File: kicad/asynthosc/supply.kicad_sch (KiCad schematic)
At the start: 51 parts, among them J1 USB_B_Micro, J17 Conn_01x02, J2 Conn_02x05_Odd_Even, U1 LM1117S-3.3, U2 LMR62421XMF, U3 USBLC6-2SC6, U4 LM1117S-5.0, U5 Si1869DH

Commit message: pcb: add design rules to match jlc pcba assembly rules. sch: fix a 0805 package mishap
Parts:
- C1, C4: footprint Capacitor_SMD:C_01005_0402Metric -> Capacitor_SMD:C_0805_2012Metric
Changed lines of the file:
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@@
 			)
 		)
-		(property "Footprint" "Capacitor_SMD:C_01005_0402Metric"
+		(property "Footprint" "Capacitor_SMD:C_0805_2012Metric"
 			(at 40.3352 96.52 0)
 			(effects
@@
 			)
 		)
-		(property "Footprint" "Capacitor_SMD:C_01005_0402Metric"
+		(property "Footprint" "Capacitor_SMD:C_0805_2012Metric"
 			(at 69.5452 96.52 0)
 			(effects

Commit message: bom: update mfr, serials and lcsc fields
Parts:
- C12, C3, C5: LCSC (none) -> C72485
- D1, D3: LCSC (none) -> C111566
- D2: LCSC (none) -> C2921026; Manufacturer Guangdong -> Agertech
- D4, D5, D6: LCSC (none) -> C3014007
- FB1: LCSC (none) -> C160974
- J1: LCSC (none) -> C5160321
- J2: LCSC (none) -> C3294463; Manufacturer (none) -> HCTL; RefNum _na_ -> PZ254-2-05-S
- L1: LCSC (none) -> C7462918
- TH1: LCSC (none) -> C2935581; Manufacturer (none) -> Ruilon; RefNum _generic_ -> NTC16D-9
- U1: LCSC (none) -> C126027
- U2: LCSC (none) -> C2070685
- U3: LCSC (none) -> C7519
- U4: LCSC (none) -> C126028
- U5: LCSC (none) -> C128638; Manufacturer (none) -> Vishay
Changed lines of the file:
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@@
 			)
 		)
-		(property "LCSC" ""
+		(property "LCSC" "C2070685 "
 			(at 59.69 190.5 0)
 			(effects
@@
 			)
 		)
-		(property "LCSC" ""
+		(property "LCSC" "C72485"
 			(at 41.91 180.34 0)
 			(effects
@@
 			)
 		)
-		(property "LCSC" ""
+		(property "LCSC" "C72485"
 			(at 80.01 259.08 0)
 			(effects
@@
 			)
 		)
-		(property "LCSC" ""
+		(property "LCSC" "C126028"
 			(at 105.41 255.27 0)
 			(effects
@@
 			)
 		)
-		(property "LCSC" ""
+		(property "LCSC" "C3014007"
 			(at 198.12 43.18 0)
 			(effects
@@
 			)
 		)
-		(property "LCSC" ""
+		(property "LCSC" "C126027"
 			(at 53.34 88.9 0)
 			(effects
@@
 			)
 		)
-		(property "LCSC" ""
+		(property "LCSC" "C128638"
 			(at 200.66 257.81 0)
 			(effects
@@
 			)
 		)
-		(property "Manufacturer" ""
+		(property "Manufacturer" "Vishay"
 			(at 200.66 257.81 0)
 			(effects
@@
 			)
 		)
-		(property "LCSC" ""
+		(property "LCSC" "C3294463"
 			(at 44.45 257.81 0)
 			(effects
@@
 			)
 		)
-		(property "Manufacturer" ""
+		(property "Manufacturer" "HCTL"
 			(at 44.45 257.81 0)
 			(effects
@@
 			)
 		)
-		(property "RefNum" "_na_"
+		(property "RefNum" "PZ254-2-05-S"
 			(at 44.45 257.81 0)
 			(effects
@@
 			)
 		)
-		(property "LCSC" ""
+		(property "LCSC" "C111566"
 			(at 67.31 57.15 0)
 			(effects
@@
 			)
 		)
-		(property "LCSC" ""
+		(property "LCSC" "C111566"
 			(at 77.47 57.15 0)
 			(effects
@@
 			)
 		)
-		(property "LCSC" ""
+		(property "LCSC" "C3014007"
 			(at 81.28 172.72 0)
 			(effects
@@
 			)
 		)
-		(property "LCSC" ""
+		(property "LCSC" "C72485"
 			(at 189.23 46.99 0)
 			(effects
@@
 			)
 		)
-		(property "RefNum" "_generic_"
+		(property "RefNum" "NTC16D-9"
 			(at 144.78 43.18 0)
 			(effects
@@
 			)
 		)
-		(property "LCSC" ""
+		(property "LCSC" "C2935581"
 			(at 144.78 43.18 0)
 			(effects
@@
 			)
 		)
-		(property "Manufacturer" ""
+		(property "Manufacturer" "Ruilon"
 			(at 144.78 43.18 0)
 			(effects
@@
 			)
 		)
-		(property "LCSC" ""
+		(property "LCSC" "C7462918"
 			(at 58.42 172.72 0)
 			(effects
@@
 			)
 		)
-		(property "LCSC" ""
+		(property "LCSC" "C7519"
 			(at 62.23 143.51 0)
 			(effects
@@
 			)
 		)
-		(property "LCSC" ""
+		(property "LCSC" "C3014007"
 			(at 133.35 248.92 0)
 			(effects
@@
 			)
 		)
-		(property "LCSC" ""
+		(property "LCSC" "C2921026"
 			(at 67.31 248.92 0)
 			(effects
@@
 			)
 		)
-		(property "Manufacturer" "Guangdong"
+		(property "Manufacturer" "Agertech"
 			(at 67.31 248.92 0)
 			(effects
@@
 			)
 		)
-		(property "LCSC" ""
+		(property "LCSC" "C160974"
 			(at 165.1 43.18 0)
 			(effects
@@
 			)
 		)
-		(property "LCSC" ""
+		(property "LCSC" "C5160321"
 			(at 40.64 43.18 0)
 			(effects

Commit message: bom: sch: pcb: update for sourcing in jlc pcba services
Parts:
- U5: LCSC C128638 -> C5246384; Manufacturer Vishay -> Tech Public; RefNum Si1869DH -> TPSI1869DH-T1-E3
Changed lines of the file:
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@@
 			)
 		)
-		(property "LCSC" "C128638"
+		(property "LCSC" "C5246384"
 			(at 200.66 257.81 0)
 			(effects
@@
 			)
 		)
-		(property "Manufacturer" "Vishay"
+		(property "Manufacturer" "Tech Public"
 			(at 200.66 257.81 0)
 			(effects
@@
 			)
 		)
-		(property "RefNum" "Si1869DH"
+		(property "RefNum" "TPSI1869DH-T1-E3"
 			(at 200.66 257.81 0)
 			(effects

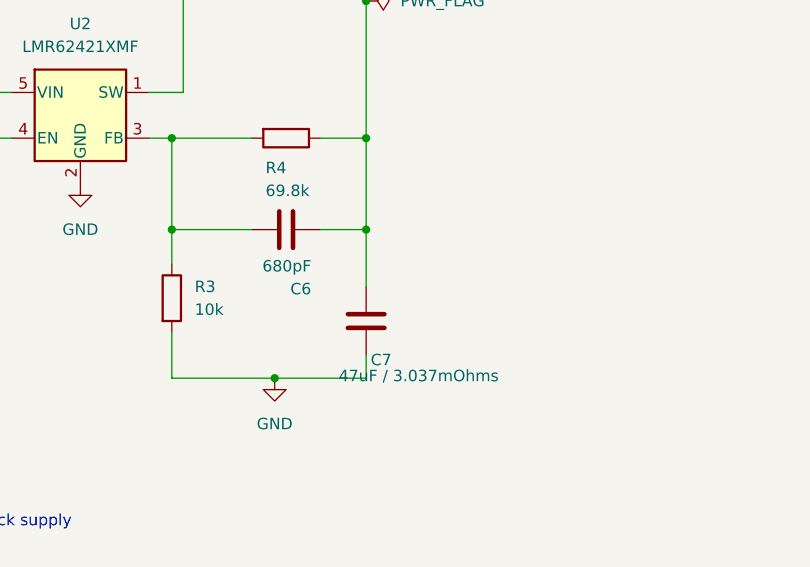
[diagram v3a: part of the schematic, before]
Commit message: bom: update for better bom
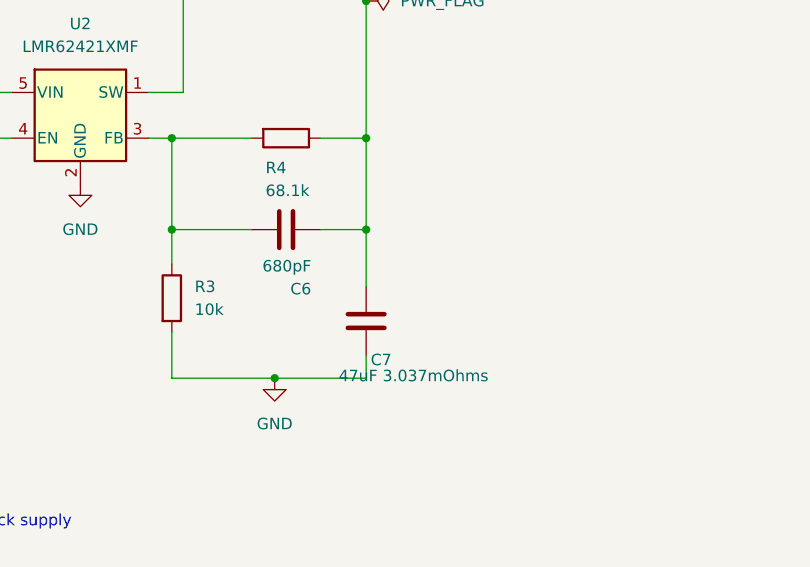
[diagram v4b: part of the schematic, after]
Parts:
- C7: value 47uF / 3.037mOhms -> 47uF 3.037mOhms
- H1, H2, H3, J17: RefNum (none) -> _na_
- R4: value 69.8k -> 68.1k
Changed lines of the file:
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@@
 			)
 		)
-		(property "Value" "47uF / 3.037mOhms"
+		(property "Value" "47uF 3.037mOhms"
 			(at 88.392 219.456 0)
 			(effects
@@
 			)
 		)
+		(property "RefNum" "_na_"
+			(at 138.43 101.6 0)
+			(effects
+				(font
+					(size 1.27 1.27)
+				)
+				(hide yes)
+			)
+		)
 		(pin "1"
 		)
@@
 			)
 		)
+		(property "RefNum" "_na_"
+			(at 106.68 73.66 0)
+			(effects
+				(font
+					(size 1.27 1.27)
+				)
+				(hide yes)
+			)
+		)
 		(pin "2"
 		)
@@
 			)
 		)
+		(property "RefNum" "_na_"
+			(at 133.35 101.6 0)
+			(effects
+				(font
+					(size 1.27 1.27)
+				)
+				(hide yes)
+			)
+		)
 		(pin "1"
 		)
@@
 			)
 		)
-		(property "Value" "69.8k"
+		(property "Value" "68.1k"
 			(at 80.264 198.882 90)
 			(effects
@@
 			(at 143.51 101.6 0)
 			(effects
+				(font
+					(size 1.27 1.27)
+				)
+				(hide yes)
+			)
+		)
+		(property "RefNum" "_na_"
+			(at 143.51 101.6 0)
+			(effects

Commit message: bom: add jlcpcb field with simplified footprint
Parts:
- C1, C2, C4, C7, C8, C9, F1: JLC (none) -> 0805
- C10, C11, C6, R1, R2, R3, R4, R5, R6: JLC (none) -> 0402
- D1, D3: JLC (none) -> SOD-923
- D2: JLC (none) -> SOD-323
- D4, D5, D6: JLC (none) -> SMA
- U1, U4: JLC (none) -> SOT-223
- U2: JLC (none) -> SOT-23-5
- U3: JLC (none) -> SOT-23-6
- U5: JLC (none) -> SOT-363

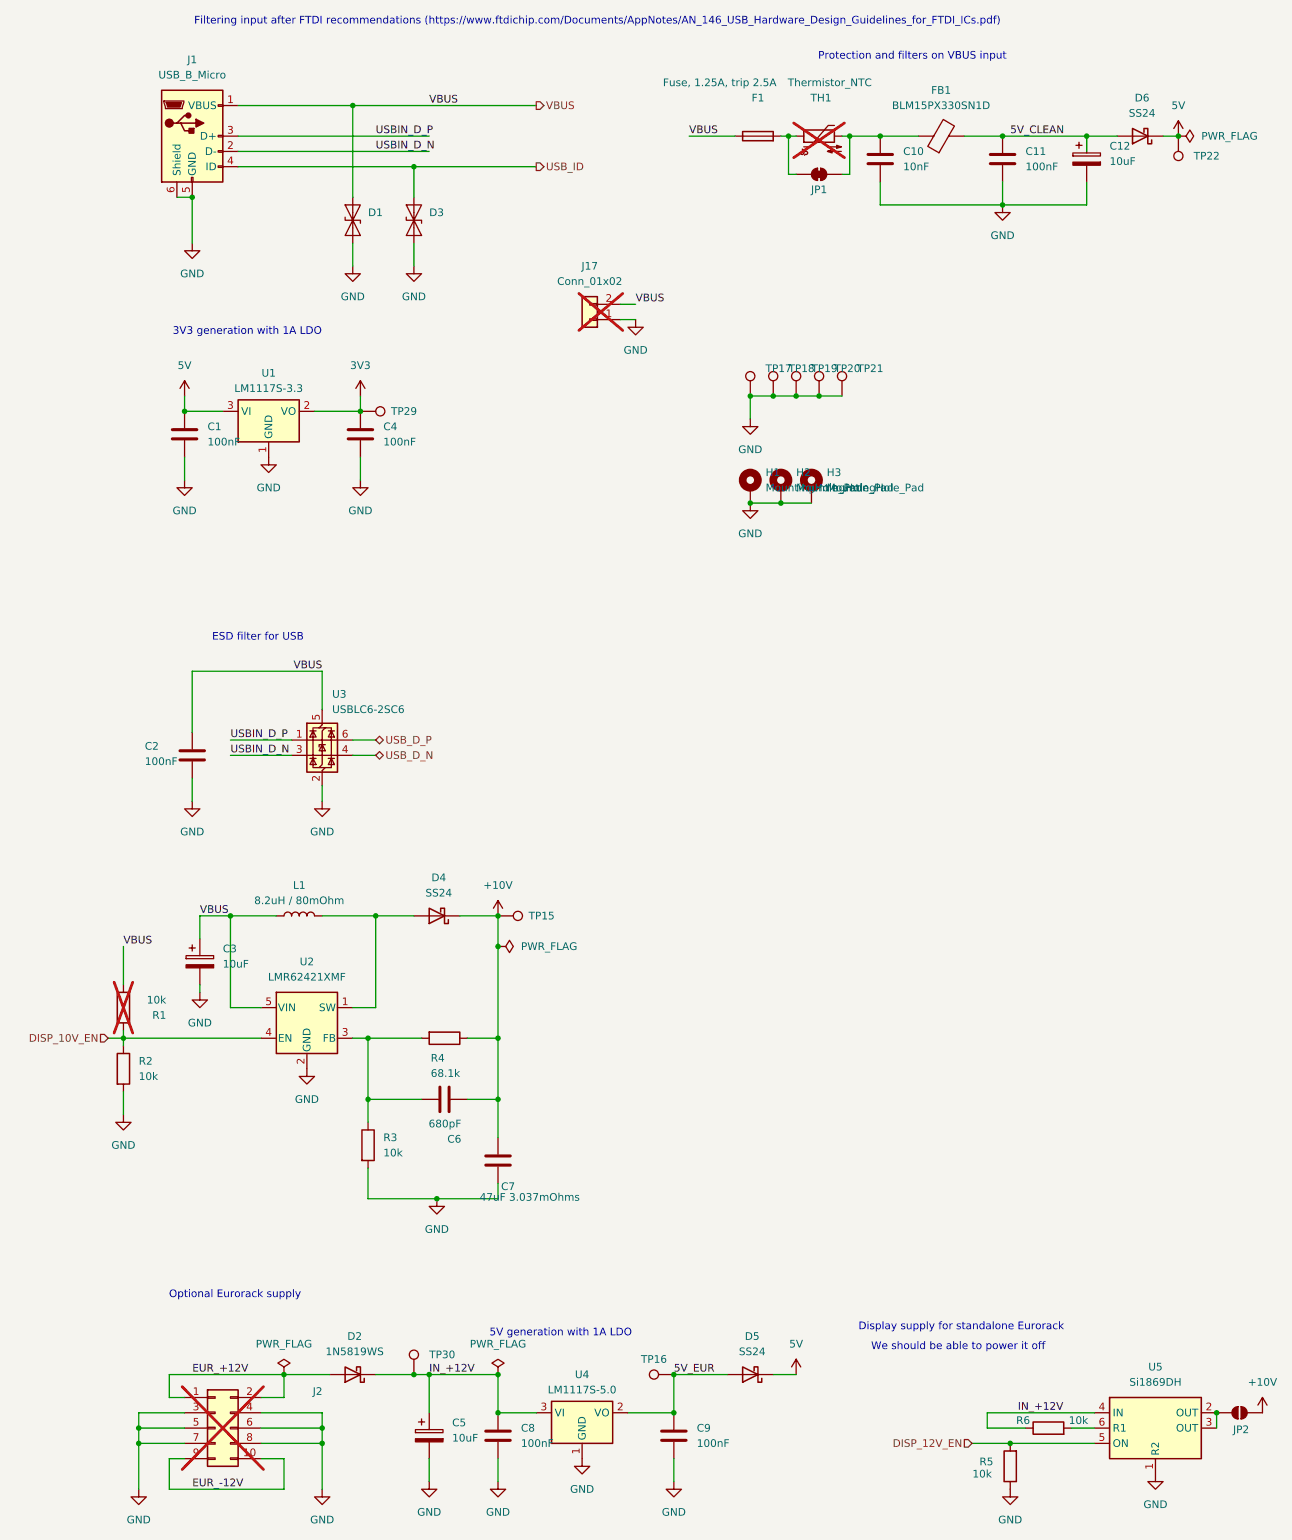
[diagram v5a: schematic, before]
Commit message: bom: dnp for all manually equiped components
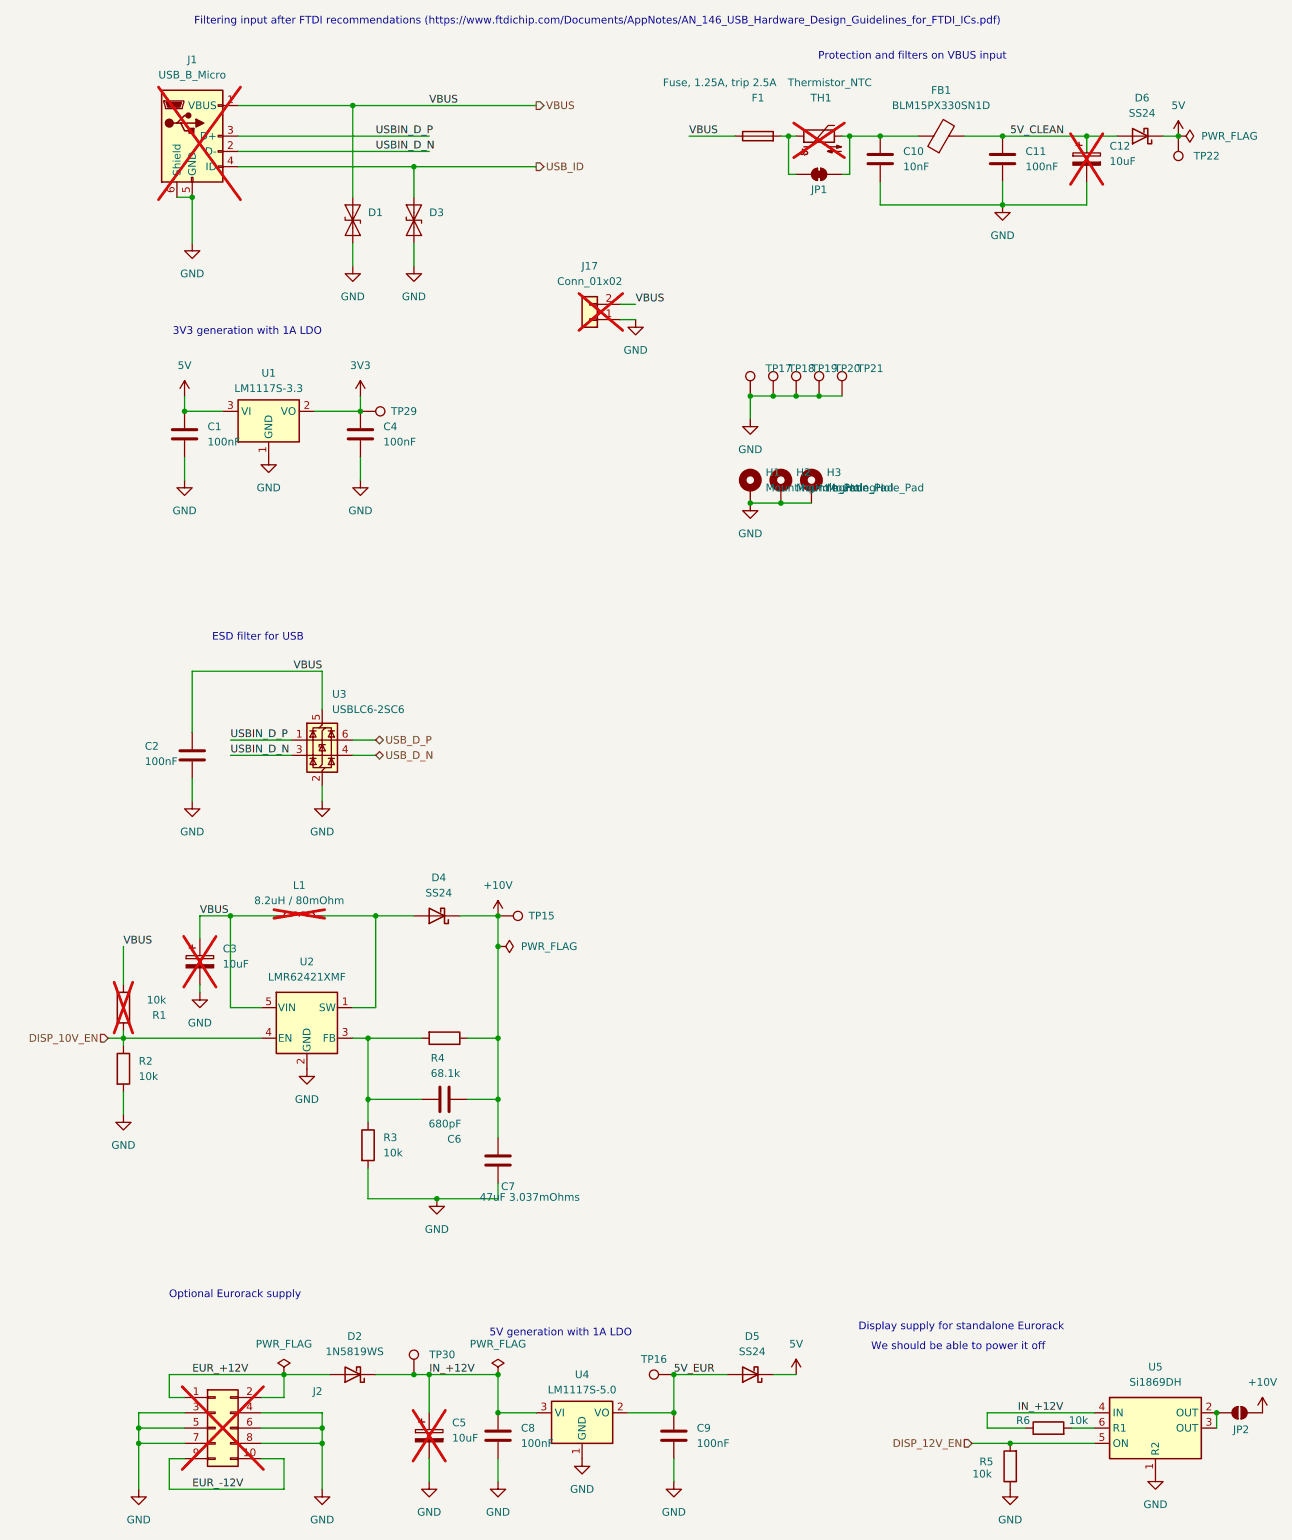
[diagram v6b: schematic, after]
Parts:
- C12, C3, C5, J1, L1: now not fitted
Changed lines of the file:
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@@
 		(in_bom yes)
 		(on_board yes)
-		(dnp no)
+		(dnp yes)
 		(fields_autoplaced yes)
 		(property "Reference" "C3"
@@
 		(in_bom yes)
 		(on_board yes)
-		(dnp no)
+		(dnp yes)
 		(fields_autoplaced yes)
 		(property "Reference" "C5"
@@
 		(in_bom yes)
 		(on_board yes)
-		(dnp no)
+		(dnp yes)
 		(fields_autoplaced yes)
 		(property "Reference" "C12"
@@
 		(in_bom yes)
 		(on_board yes)
-		(dnp no)
+		(dnp yes)
 		(fields_autoplaced yes)
 		(property "Reference" "L1"
@@
 		(in_bom yes)
 		(on_board yes)
-		(dnp no)
+		(dnp yes)
 		(fields_autoplaced yes)
 		(property "Reference" "J1"

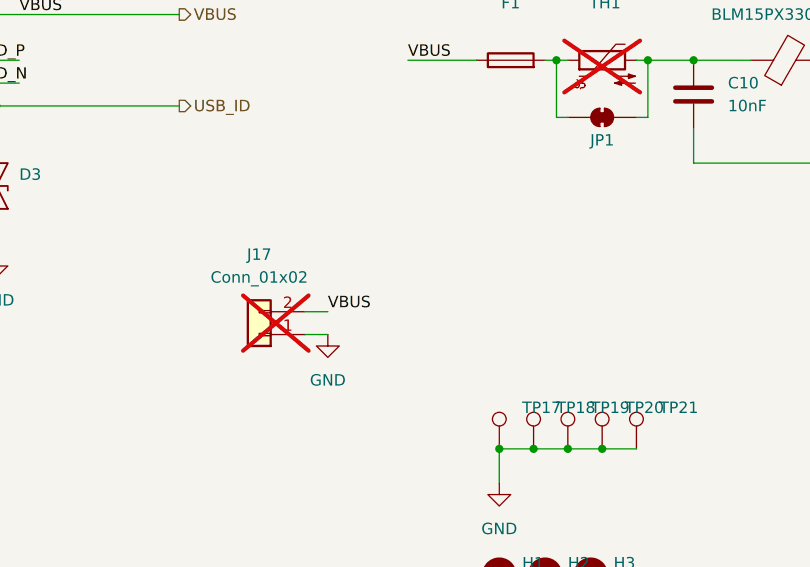
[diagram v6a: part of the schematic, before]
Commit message: sch: pcb: add a diode for external 5V input to protect USB VBUS
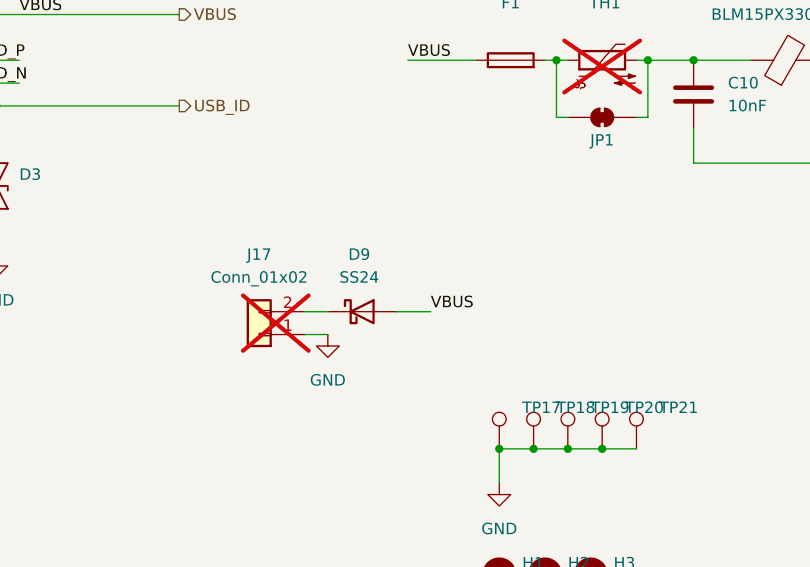
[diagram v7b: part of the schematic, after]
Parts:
- added D9: SS24, Diode_SMD:D_SMA, symbol Diode:SS24
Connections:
- net VBUS: now also D9.2 (A); no longer J17.2 (Pin_2)
- new net: D9.1 (K), J17.2 (Pin_2)
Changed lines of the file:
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@@
 	(wire
 		(pts
+			(xy 125.73 71.12) (xy 121.92 71.12)
+		)
+		(stroke
+			(width 0)
+			(type default)
+		)
+	)
+	(wire
+		(pts
 			(xy 91.44 203.2) (xy 91.44 209.55)
 		)
@@
 	)
 	(label "VBUS"
+		(at 125.73 71.12 0)
+		(fields_autoplaced yes)
+		(effects
+			(font
+				(size 1.27 1.27)
+			)
+			(justify left bottom)
+		)
+	)
+	(label "VBUS"
 		(at 29.21 177.8 0)
 		(fields_autoplaced yes)
@@
 	)
 	(label "VBUS"
-		(at 114.3 71.12 0)
-		(fields_autoplaced yes)
-		(effects
-			(font
-				(size 1.27 1.27)
-			)
-			(justify left bottom)
-		)
-	)
-	(label "VBUS"
 		(at 80.01 38.1 0)
 		(fields_autoplaced yes)
@@
 					(unit 1)
 				)
+			)
+		)
+	)
+	(symbol
+		(lib_id "Diode:SS24")
+		(at 118.11 71.12 0)
+		(unit 1)
+		(exclude_from_sim no)
+		(in_bom yes)
+		(on_board yes)
+		(dnp no)
+		(fields_autoplaced yes)
+		(property "Reference" "D9"
+			(at 117.7925 64.77 0)
+			(effects
+				(font
+					(size 1.27 1.27)
+				)
+			)
+		)
+		(property "Value" "SS24"
+			(at 117.7925 67.31 0)
+			(effects
+				(font
+					(size 1.27 1.27)
+				)
+			)
+		)
+		(property "Footprint" "Diode_SMD:D_SMA"
+			(at 118.11 75.565 0)
+			(effects
+				(font
+					(size 1.27 1.27)
+				)
+				(hide yes)
+			)
+		)
+		(property "Datasheet" "https://www.vishay.com/docs/88748/ss22.pdf"
+			(at 118.11 71.12 0)
+			(effects
+				(font
+					(size 1.27 1.27)
+				)
+				(hide yes)
+			)
+		)
+		(property "Description" "40V 2A Schottky Diode, SMA"
+			(at 118.11 71.12 0)
+			(effects
+				(font
+					(size 1.27 1.27)
+				)
+				(hide yes)
+			)
+		)
+		(property "LCSC" "C3014007"
+			(at 118.11 71.12 0)
+			(effects
+				(font
+					(size 1.27 1.27)
+				)
+				(hide yes)
+			)
+		)
+		(property "Manufacturer" "Fosan"
+			(at 118.11 71.12 0)
+			(effects
+				(font
+					(size 1.27 1.27)
+				)
+				(hide yes)
+			)
+		)
+		(property "RefNum" "SS24"
+			(at 118.11 71.12 0)
+			(effects
+				(font
+					(size 1.27 1.27)
+				)
+				(hide yes)
+			)
+		)
+		(property "JLC" "SMA"
+			(at 118.11 71.12 0)
+			(effects
+				(font
+					(size 1.27 1.27)
+				)
+				(hide yes)
+			)
+		)
+		(pin "1"
+		)
+		(pin "2"
+		)
+		(instances
+			(project "asynthosc"
+				(path "/d73e377a-a016-415f-8824-91cc6e4907b9/22ca5166-338c-4a24-8f8a-545e4a0286bf"
+					(reference "D9")
+					(unit 1)
+				)
